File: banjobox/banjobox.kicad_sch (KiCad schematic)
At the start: 8 parts, among them SW1 RotaryEncoder_Switch, U1 SHT31-DIS, U2 MOUDLE-SEEEDUINO-XIAO, U3 ER_OLEDM0.91_1x-I2C, U4 PAM8302AAY

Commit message: first draft of schematic
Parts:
- added C1: 1uF, symbol Device:C_Polarized
- added C2: 10uf, symbol Device:C_Polarized
- added C3: 0.1uF, symbol Device:C
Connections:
- net GND: now also U4.4 (IN-), U4.7 (GND), C1.2, C2.2
- net VCC: now also U4.6 (VDD), C1.1, C2.1
- net at U4.3 (IN+): now also C3.2
- net AUDIO: now reaches U2.4 (PA11_A3_D3)
- net AUDIO: now also C3.1
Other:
- note added: "Amplifier and speaker"
- note added: "Encoder"
- note added: "OLED display"
- note added: "Temp/ Humidity sensor"
- moved on the sheet: LS1, R1, R2, SW1, U1, U2, U3, U4

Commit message: uploaded pcb workflow, copied from chatgpt. made minor change to schematic.
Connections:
- net GND: now also U1.2 (ADDR)
- net VCC: no longer U1.2 (ADDR)
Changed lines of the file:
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@@
-	)
-	(junction
-		(at 50.8 72.39)
-		(diameter 0)
-		(color 0 0 0 0)
-	)
-	(junction
-		(at 50.8 93.98)
-		(diameter 0)
-		(color 0 0 0 0)
 	)
 	(junction
@@
 	(wire
 		(pts
-			(xy 50.8 68.58) (xy 50.8 72.39)
-		)
-		(stroke
-			(width 0)
-			(type default)
-		)
-	)
-	(wire
-		(pts
 			(xy 40.64 146.05) (xy 50.8 146.05)
 		)
@@
 	(wire
 		(pts
-			(xy 50.8 72.39) (xy 50.8 76.2)
-		)
-		(stroke
-			(width 0)
-			(type default)
-		)
-	)
-	(wire
-		(pts
-			(xy 40.64 81.28) (xy 36.83 81.28)
+			(xy 30.48 81.28) (xy 40.64 81.28)
+		)
+		(stroke
+			(width 0)
+			(type default)
+		)
+	)
+	(wire
+		(pts
+			(xy 50.8 68.58) (xy 50.8 76.2)
 		)
 		(stroke
@@
 	(wire
 		(pts
-			(xy 36.83 93.98) (xy 50.8 93.98)
-		)
-		(stroke
-			(width 0)
-			(type default)
-		)
-	)
-	(wire
-		(pts
 			(xy 251.46 111.76) (xy 251.46 114.3)
 		)
@@
 	(wire
 		(pts
-			(xy 50.8 91.44) (xy 50.8 93.98)
-		)
-		(stroke
-			(width 0)
-			(type default)
-		)
-	)
-	(wire
-		(pts
-			(xy 36.83 81.28) (xy 36.83 72.39)
+			(xy 50.8 91.44) (xy 50.8 96.52)
 		)
 		(stroke
@@
 	(wire
 		(pts
-			(xy 50.8 93.98) (xy 50.8 96.52)
-		)
-		(stroke
-			(width 0)
-			(type default)
-		)
-	)
-	(wire
-		(pts
 			(xy 40.64 86.36) (xy 36.83 86.36)
-		)
-		(stroke
-			(width 0)
-			(type default)
-		)
-	)
-	(wire
-		(pts
-			(xy 36.83 72.39) (xy 50.8 72.39)
 		)
 		(stroke
@@
 	(symbol
 		(lib_id "power:GND")
+		(at 36.83 93.98 0)
+		(unit 1)
+		(body_style 1)
+		(exclude_from_sim no)
+		(in_bom yes)
+		(on_board yes)
+		(in_pos_files yes)
+		(dnp no)
+		(fields_autoplaced yes)
+		(property "Reference" "#PWR016"
+			(at 36.83 100.33 0)
+			(hide yes)
+			(show_name no)
+			(do_not_autoplace no)
+			(effects
+				(font
+					(size 1.27 1.27)
+				)
+			)
+		)
+		(property "Value" "GND"
+			(at 36.83 99.06 0)
+			(show_name no)
+			(do_not_autoplace no)
+			(effects
+				(font
+					(size 1.27 1.27)
+				)
+			)
+		)
+		(property "Footprint" ""
+			(at 36.83 93.98 0)
+			(hide yes)
+			(show_name no)
+			(do_not_autoplace no)
+			(effects
+				(font
+					(size 1.27 1.27)
+				)
+			)
+		)
+		(property "Datasheet" ""
+			(at 36.83 93.98 0)
+			(hide yes)
+			(show_name no)
+			(do_not_autoplace no)
+			(effects
+				(font
+					(size 1.27 1.27)
+				)
+			)
+		)
+		(property "Description" "Power symbol creates a global label with name \"GND\" , ground"
+			(at 36.83 93.98 0)
+			(hide yes)
+			(show_name no)
+			(do_not_autoplace no)
+			(effects
+				(font
+					(size 1.27 1.27)
+				)
+			)
+		)
+		(pin "1"
+		)
+		(instances
+			(project "banjobox"
+				(path "/e9efcbc3-04d6-4368-adc8-7837a0480666"
+					(reference "#PWR016")
+					(unit 1)
+				)
+			)
+		)
+	)
+	(symbol
+		(lib_id "power:GND")
 		(at 153.67 111.76 0)
 		(unit 1)
@@
 					(unit 1)
 				)
+			)
+		)
+	)
+	(symbol
+		(lib_id "power:GND")
+		(at 30.48 81.28 0)
+		(unit 1)
+		(body_style 1)
+		(exclude_from_sim no)
+		(in_bom yes)
+		(on_board yes)
+		(in_pos_files yes)
+		(dnp no)
+		(fields_autoplaced yes)
+		(property "Reference" "#PWR015"
+			(at 30.48 87.63 0)
+			(hide yes)
+			(show_name no)
+			(do_not_autoplace no)
+			(effects
+				(font
+					(size 1.27 1.27)
+				)
+			)
+		)
+		(property "Value" "GND"
+			(at 30.48 86.36 0)
+			(show_name no)
+			(do_not_autoplace no)
+			(effects
+				(font
+					(size 1.27 1.27)
+				)
+			)
+		)
+		(property "Footprint" ""
+			(at 30.48 81.28 0)
+			(hide yes)
+			(show_name no)
+			(do_not_autoplace no)
+			(effects
+				(font
+					(size 1.27 1.27)
+				)
+			)
+		)
+		(property "Datasheet" ""
+			(at 30.48 81.28 0)
+			(hide yes)
+			(show_name no)
+			(do_not_autoplace no)
+			(effects
+				(font
+					(size 1.27 1.27)
+				)
+			)
+		)
+		(property "Description" "Power symbol creates a global label with name \"GND\" , ground"
+			(at 30.48 81.28 0)
+			(hide yes)
+			(show_name no)
+			(do_not_autoplace no)
+			(effects
+				(font
+					(size 1.27 1.27)
+				)
+			)
+		)
+		(pin "1"
+		)
+		(instances
+			(project "banjobox"
+				(path "/e9efcbc3-04d6-4368-adc8-7837a0480666"
+					(reference "#PWR015")
+					(unit 1)
+				)

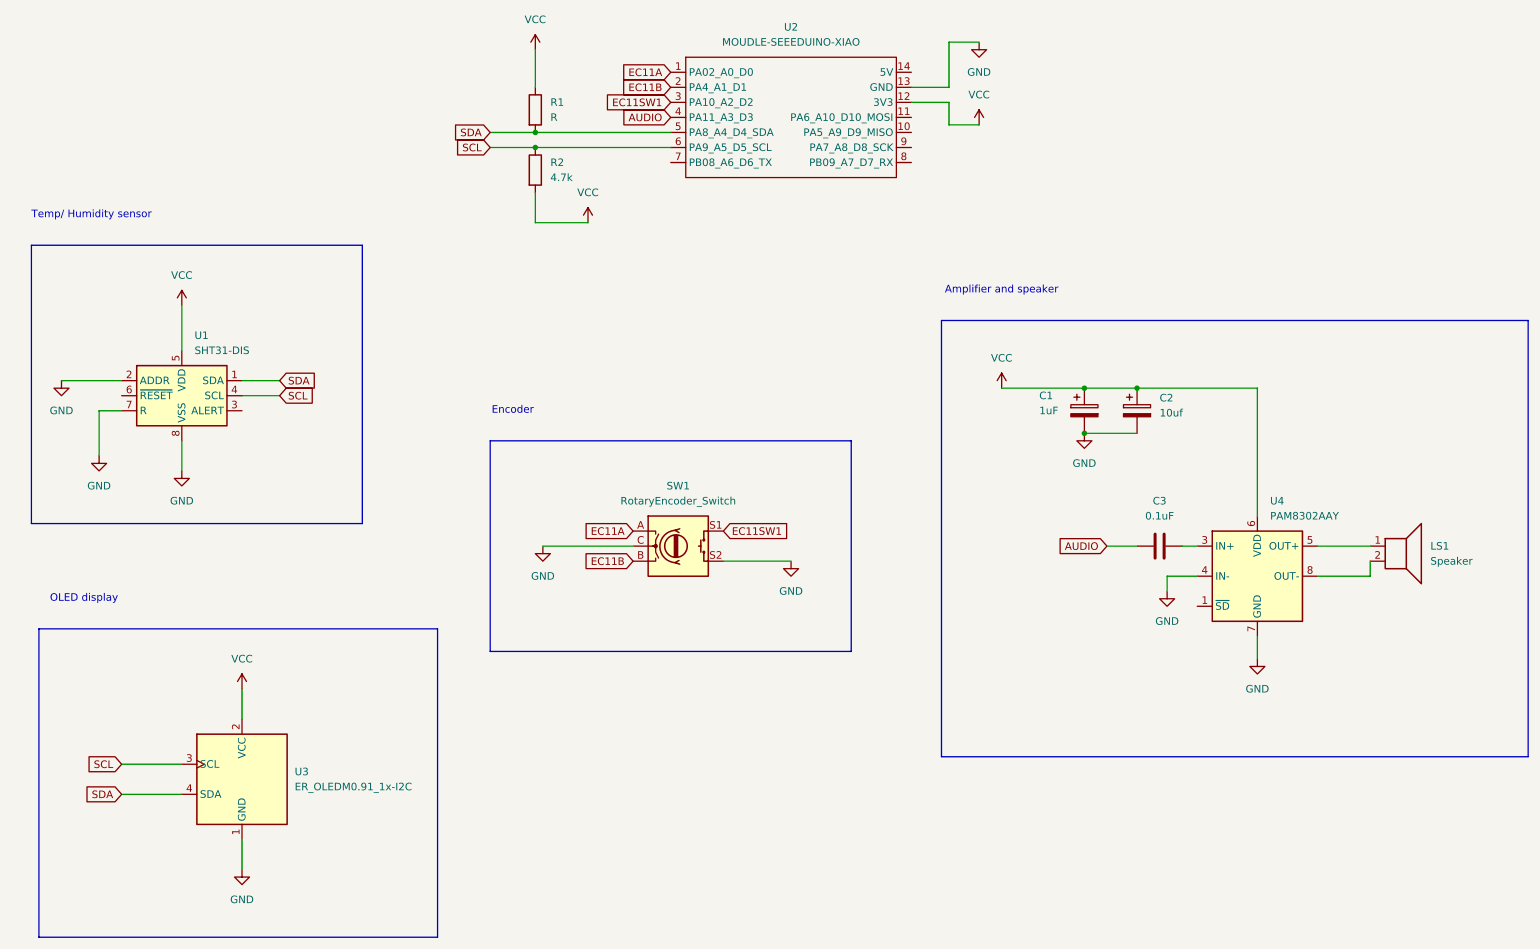
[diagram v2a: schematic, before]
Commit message: completed drawing schematic
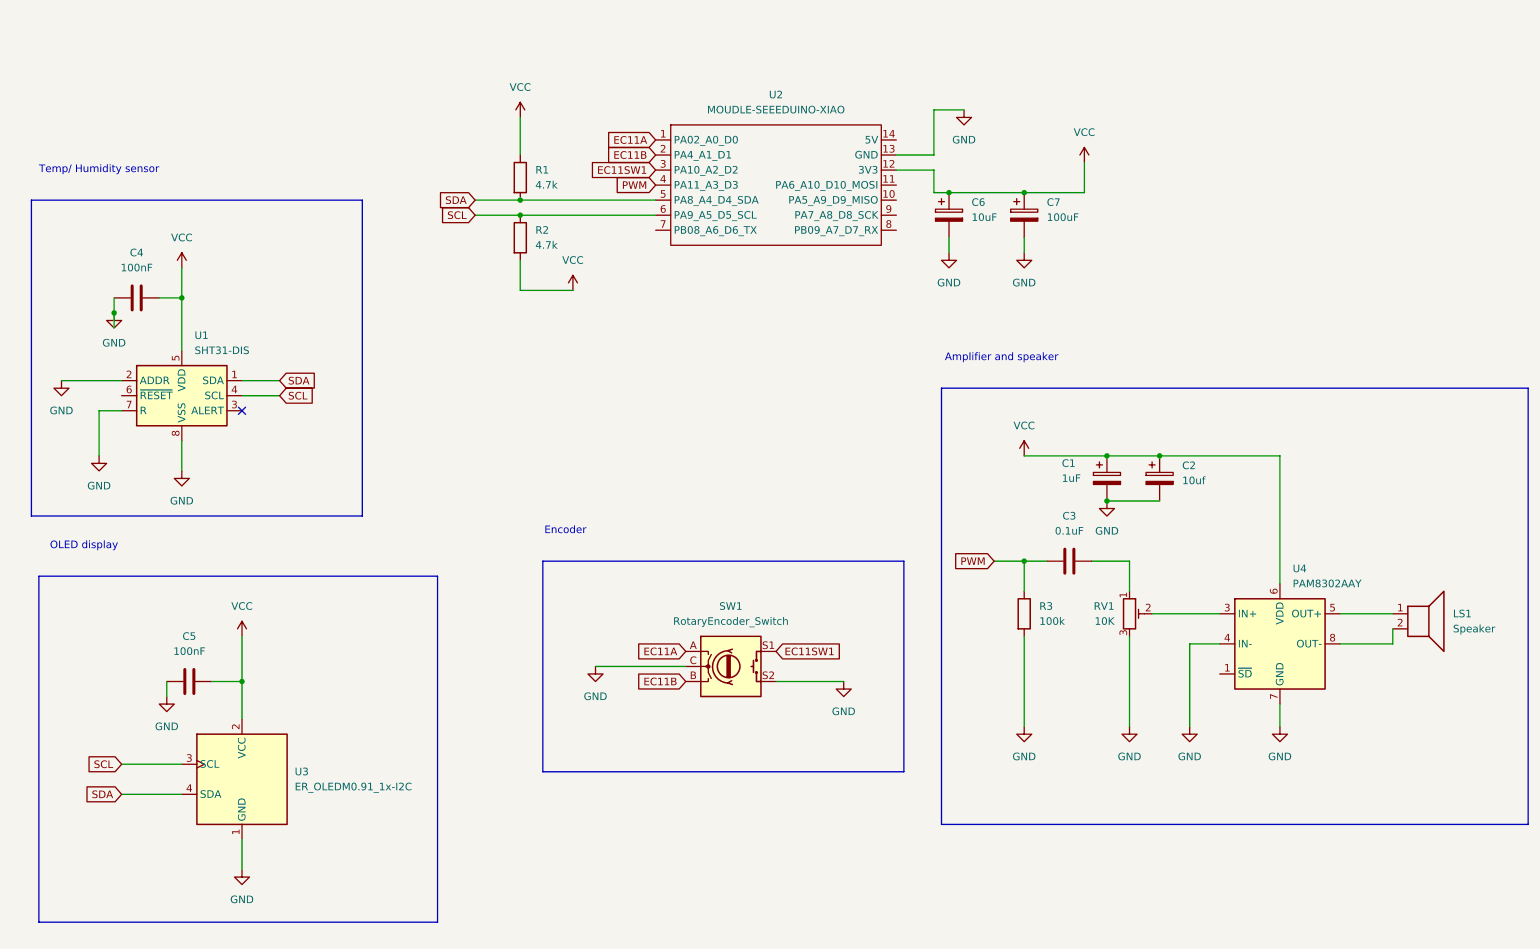
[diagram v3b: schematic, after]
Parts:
- added C4, C5: 100nF, symbol Device:C
- added C6: 10uF, symbol Device:C_Polarized
- added C7: 100uF, symbol Device:C_Polarized
- added R3: 100k, symbol Device:R
- added RV1: 10K, symbol Device:R_Potentiometer_Trim
- R1: value R -> 4.7k
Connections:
- net GND: now also C4.1, C5.1, C6.2, C7.2, R3.2, RV1.3
- net VCC: now also C4.2, C5.2, C6.1, C7.1
- net at C3.2: now also RV1.1; no longer U4.3 (IN+)
- net AUDIO renamed PWM
- net PWM: now also R3.1
- new net: RV1.2, U4.3 (IN+)
- no-connect marks 0 -> 1
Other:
- moved on the sheet: C1, C2, C3, LS1, R1, R2, SW1, U2, U4
